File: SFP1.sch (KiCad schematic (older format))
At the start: 20 parts, among them J3 TYCO_1888247-1

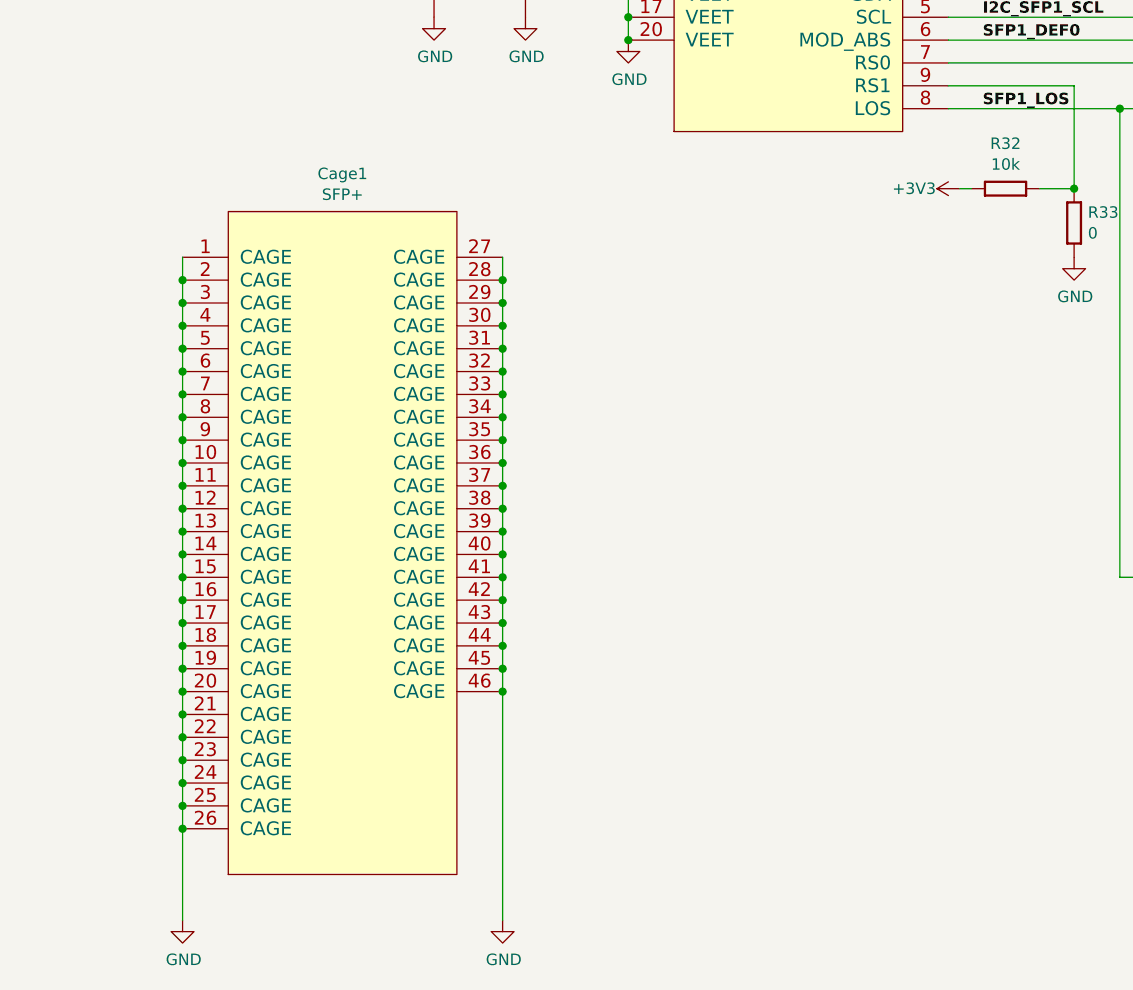
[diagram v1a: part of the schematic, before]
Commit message: FMC HPC & LPC done, FPGA power delivery done, RGMII lines done,  MGT lines progress
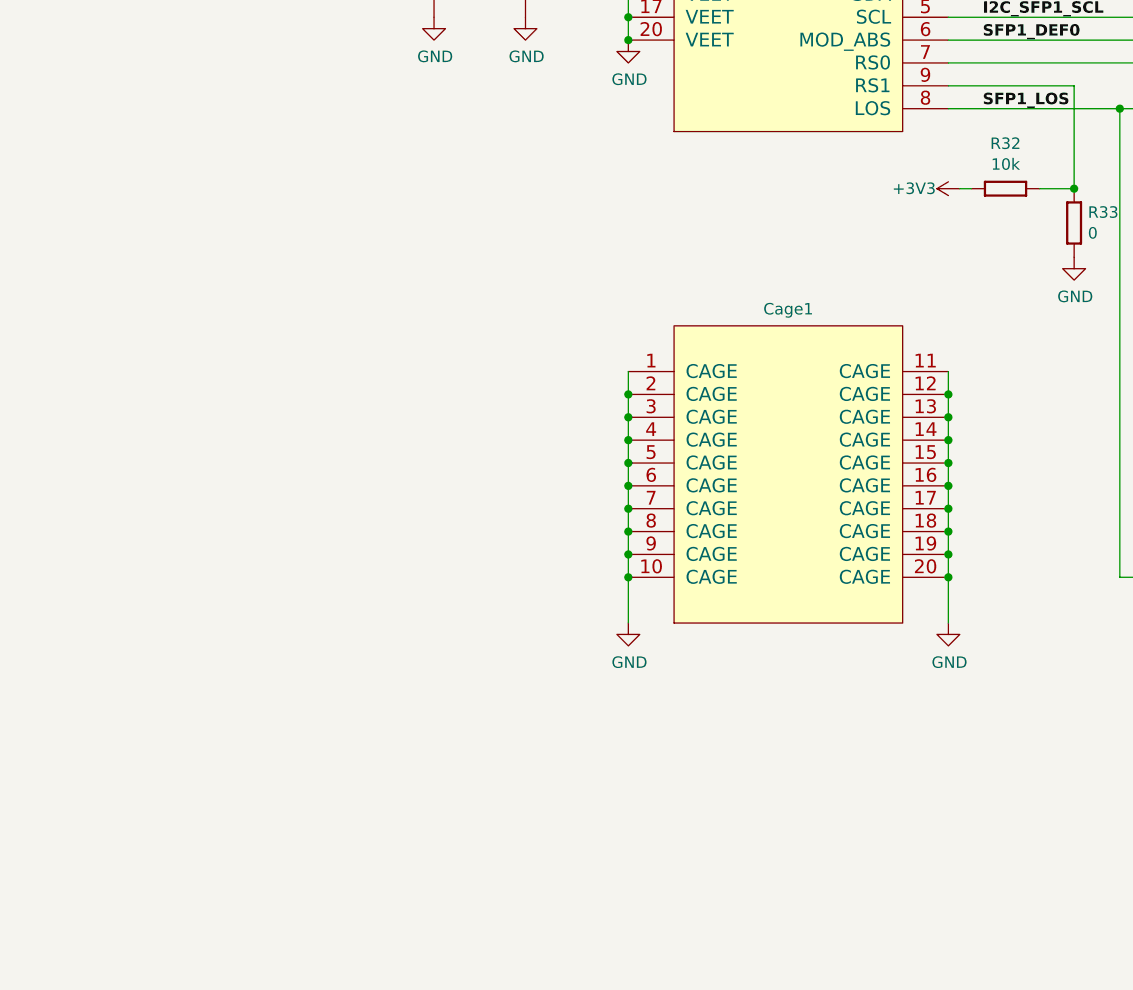
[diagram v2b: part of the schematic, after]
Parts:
- removed Cage1: TYCO_2007132-1, TYCO THD:TYCO_2007132-1, symbol TYCO:TYCO_2007132-1
- added Cage1: TYCO_2007198-1, TYCO THD:TYCO_2007198-1, symbol TYCO:TYCO_2007198-1
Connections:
- net GND: now also Cage1.1 (CAGE), Cage1.10 (CAGE), Cage1.11 (CAGE), Cage1.12 (CAGE), Cage1.13 (CAGE), Cage1.14 (CAGE), Cage1.15 (CAGE), Cage1.16 (CAGE), Cage1.17 (CAGE), Cage1.18 (CAGE), Cage1.19 (CAGE), Cage1.2 (CAGE), Cage1.20 (CAGE), Cage1.3 (CAGE), Cage1.4 (CAGE), Cage1.5 (CAGE), Cage1.6 (CAGE), Cage1.7 (CAGE), Cage1.8 (CAGE), Cage1.9 (CAGE)
